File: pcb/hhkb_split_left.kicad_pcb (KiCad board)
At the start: 4 copper layers, 140.4 x 97.4 mm, 68 parts, among them SW1 Esc, SW10 E, SW11 R, SW12 T, SW13 Ctrl, SW14 A, SW15 S, SW16 D, SW17 F, SW18 G, SW19 Shift, SW2 1, SW20 Z, SW21 X, SW22 C, SW23 V, SW24 B, SW25 Alt, SW26 Meta, SW27 L-Space, SW3 2, SW4 3, SW5 4, SW6 5, SW7 Tab, SW8 Q, SW9 W, U1 74LVC595

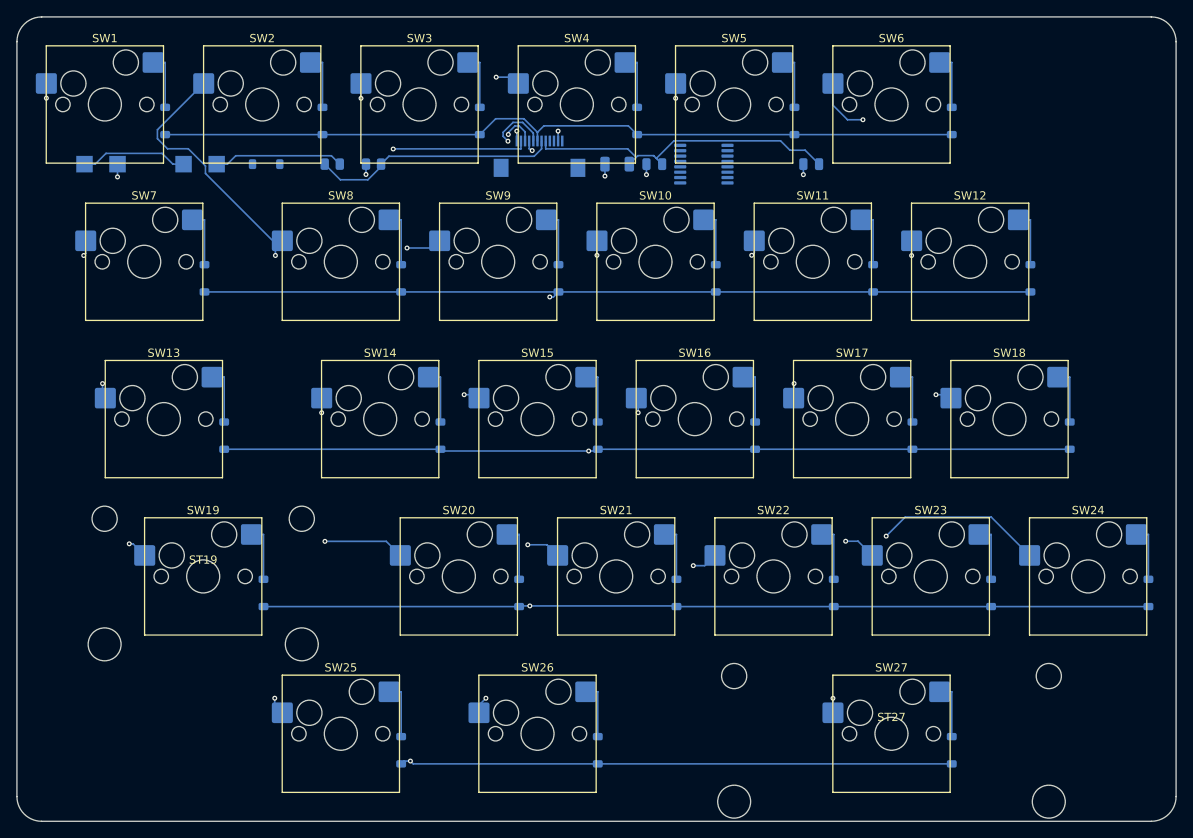
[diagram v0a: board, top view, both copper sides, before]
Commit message: マトリクスのダイオードを BAT46W にした（1N4148W はバックアップとして記録）
在庫 5,000 超の SOD-123 ショットキー 29 件、BAT47/48/49/54/85、1SS 系、
NSR、RB751、PMEG、MBR05xx、SS12、1N5711、BAS40 を当たった。
**VF と IR を両方「動作点で」保証しているのは BAT46W だけ。**

  BAT46W(C54110)  VF≦0.25V@0.1mA   IR≦0.3µA@1.5V   $6.76(122個+段取り)
  1N4148W(C81598) なし(1mA 0.715V) なし(20V 25nA)  $1.43 Basic
  SD103AW         0.37V@20mA       なし(30V 5µA)   $6.75
  BAT54W          240mV@0.1mA      なし(25V 2µA)   $6.25

罠: BAT48ZFILM-FS(C7436546) は名前だけで中身は SD103AW と同じ仕様。

## 効果

打ち止めがマイコン律速に戻る（1.20 → **1.10V/本**）。
**壊れ方が「一部のキーが反応しない」から「電源が落ちる」に変わる。**
実測が不要になる。

## 代償（数字で押さえた）

+約 ¥800。逆漏れ 12 倍で **60℃ かつ 5 個以上の同時押しだと余裕を割る**
（25℃ なら 9 個でも OK）。接合容量 5 倍だが列切替後 2.31µs に対し
SPI 転送で 4.0µs 以上空くので間に合う。

## 検査を 2 つ足した

  test_the_matrix_reads_high_at_the_cutoff … 打ち止めで行が VIH に届くか
  test_ghosting_survives_a_full_row_of_simultaneous_presses … 逆漏れの合計

どちらも故意に壊して検出を確認した。**1 回目は __pycache__ が古いまま
（同じ秒に書き換えたため）で検出できていなかった。**破壊試験のあとは
バイトコードを消すこと。

open-gaps #25 に「電池が尽きるときの止まり方」を記録した。マイコンの
ブラウンアウトは起動と広告を繰り返しうるし、**低電圧の flash 書き込みで
ペアリング情報が壊れうる**。POFCON か soft-off で自分から止めれば直るが、
ZMK に機能が無いので自作が要る。**基板に影響しないので届いてからでよい。**

3 基板とも DRC 0 / 未配線 0。検査 294 件。

Co-Authored-By: Claude Opus 5 (1M context) <noreply@anthropic.com>
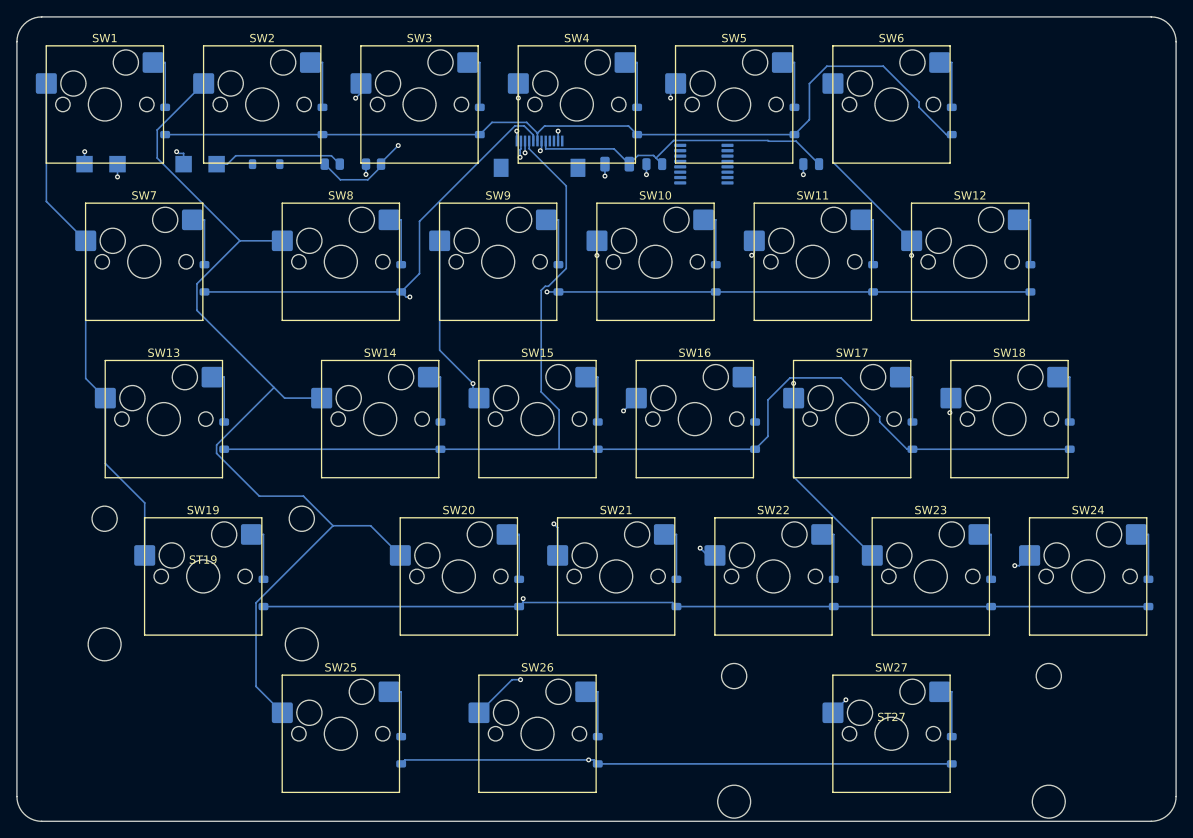
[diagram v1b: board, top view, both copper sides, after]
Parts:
- D1, D10, D11, D12, D13, D14, D15, D16, D17, D18, D19, D2, D20, D21, D22, D23, D24, D25, D26, D27, D3, D4, D5, D6, D7, D8, D9: value 1N4148W -> BAT46W
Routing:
- net COL1: track 104.3 -> 126.8 mm, vias 4 -> 0
- net COL2: track 74.7 -> 88.6 mm, vias 4 -> 3
- net ROW2: track 143.5 -> 154.1 mm, vias 2 -> 0
- net ROW0: track 98.5 -> 107.9 mm
- net ROW4: track 159.7 -> 151.4 mm
- net COL5: track 111.6 -> 104.9 mm, vias 5 -> 4
- net COL3: track 112.1 -> 105.6 mm
- net ROW3: track 174.0 -> 168.8 mm
- net COL0: track 66.1 -> 62.1 mm, vias 4 -> 0
- net COL4: track 71.6 -> 69.4 mm, vias 4 -> 3
- net VBATT_RAW: track 13.1 -> 14.9 mm, vias 0 -> 2
- net VBATT_SENSE: track 29.7 -> 30.4 mm, vias 0 -> 2

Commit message: #23 の D9 移設を実施した（アンテナ実外形の真下の配線が 0 本になった）
- ROW4 の行き先を D5（左列）→ D9（右列・元 MISO）へ。TX 側レーン 6 → 5 本、
  LANE_STEP 0.7 → 0.65。最内レーン -3.8mm はアンテナ実外形（-3.65〜-0.15）の外
- ケーブルのピン配置は ROW4 を右群 4 番へ（左群のままだと横枝が縦線を
  8 箇所で横切る。DRC で実測）。本体基板 2 枚も再生成＋再配線。3 基板 DRC 0
- ファームは row-gpios を D9 へ、&spi2_default/&spi2_sleep の psels から
  MISO を外して P1.14 を解放（CI ビルド・実機は未確認）
- 買い物リストを shopping-list.md に統合（#22 の再発防止の作法つき）
- Task C3 §6-6b に測定条件欄を追加
- 全検査 386 passed / 3 skipped

Co-Authored-By: Claude Fable 5 <noreply@anthropic.com>
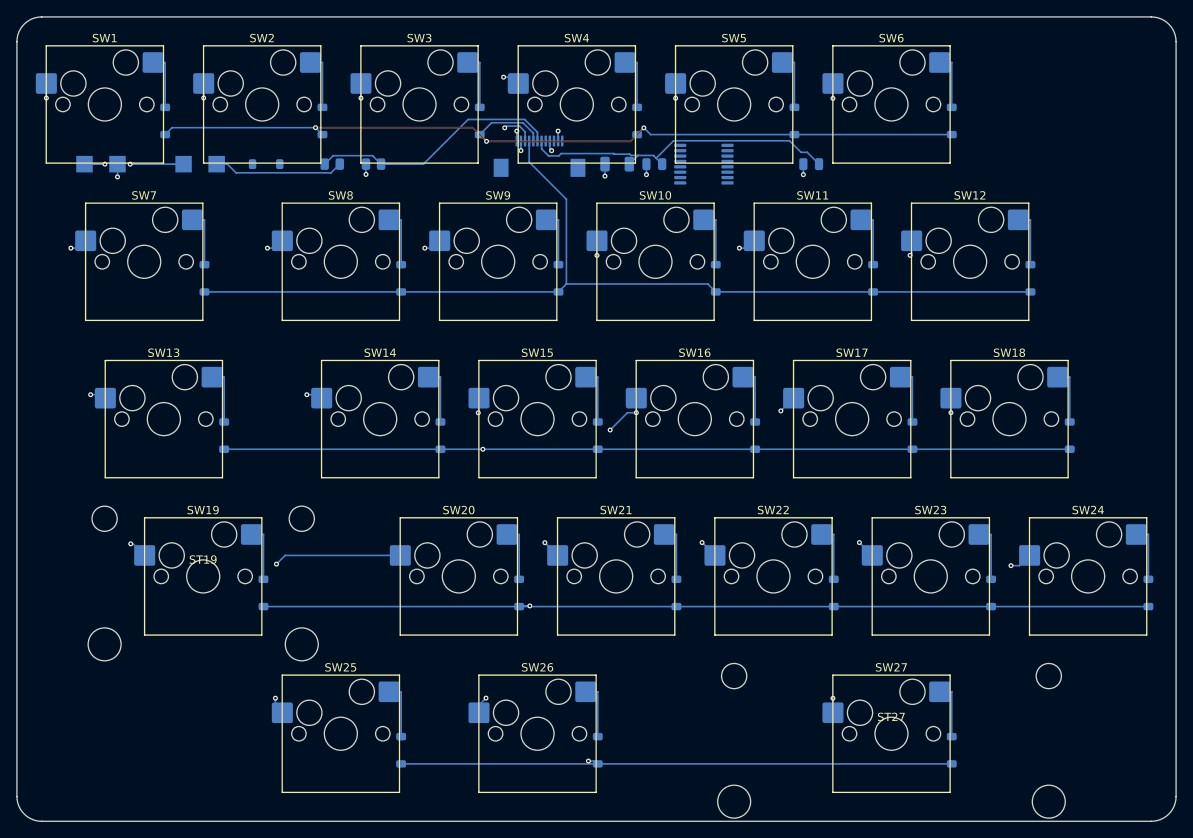
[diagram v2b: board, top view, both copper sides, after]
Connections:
- J_DB pad 10: ROW3 -> ROW2
- J_DB pad 11: ROW4 -> ROW3
- J_DB pad 4: SPI_MOSI -> ROW4
- J_DB pad 5: V3V3 -> SPI_MOSI
- J_DB pad 6: VBATT_SENSE -> V3V3
- J_DB pad 7: ROW0 -> VBATT_SENSE
- J_DB pad 8: ROW1 -> ROW0
- J_DB pad 9: ROW2 -> ROW1
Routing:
- net COL1: track 126.8 -> 102.9 mm, vias 0 -> 5
- net COL2: track 88.6 -> 71.1 mm, vias 3 -> 4
- net ROW1: track 129.7 -> 120.0 mm, vias 2 -> 0
- net COL3: track 105.6 -> 113.3 mm, vias 5 -> 6
- net ROW4: track 151.4 -> 156.9 mm
- net ROW2: track 154.1 -> 149.6 mm, vias 0 -> 2
- net COL0: track 62.1 -> 66.4 mm, vias 0 -> 4
- net VBATT_RAW: track 14.9 -> 12.0 mm
- net COL4: track 69.4 -> 71.4 mm, vias 3 -> 4
- net ROW0: track 107.9 -> 109.3 mm, vias 0 -> 3
- net V3V3: track 38.5 -> 39.8 mm
- net COL5: track 104.9 -> 103.6 mm, vias 4 -> 5
- net ROW3: track 168.8 -> 169.8 mm
- net VBATT_SENSE: track 30.4 -> 30.5 mm, vias 2 -> 0

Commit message: ★ 電池蓋を差し込み式にし、本体基板に固定を入れた（#35 / #36）
電池蓋（#35）: コブの奥面へ移し、留め方を 3 度作り直した。片持ちばね案は
**原理的に外れない**（腕が壁の裏に立っていて、どう撓ませても抜けない。
逃がす先の内側は電池が埋めている）。断面を描いて分かった。採用したのは
下へスライドして庇の裏へ舌を差し込む形で、重力が留める側に効く。
検査は「留まる」と「外せる」を必ず一緒に見る——前者だけでは不成立案が通った。

本体基板（#36）: 取付穴 6/8 とプレート裏の柱・M2 ネジ。穴の探索が
コートヤードしか見ておらず、柱がキーとプレート開口に当たっていた。
柱の検査は assert がループの中にあって 1 本目で止まっており、3 往復した。

その他: 自動配線器がたまに 0.12mm の線を引いて DRC が赤になるので、
取り込み後に幅を揃えるようにした（配線するたびに赤が出たり出なかったり
していた）。CAD を変えたら絵を出し直す手順を tools/refresh_view.sh に。

検査 395 件 緑 / DRC 3 基板とも 0 違反・0 未配線

Co-Authored-By: Claude Opus 5 (1M context) <noreply@anthropic.com>
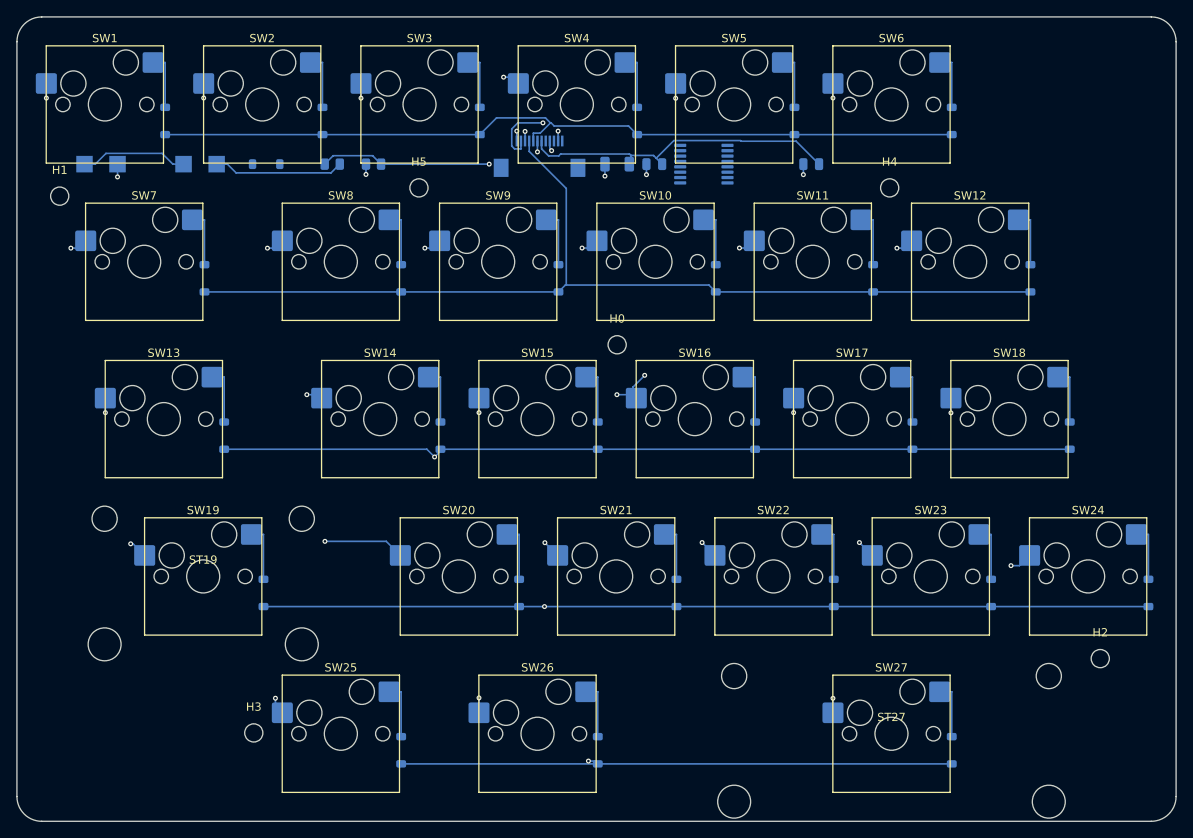
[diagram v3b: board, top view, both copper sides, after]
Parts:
- added H0: MountingHole_2.2mm_M2, MountingHole_2.2mm_M2, F.Cu at (152.5, 91.0)
- added H1: MountingHole_2.2mm_M2, MountingHole_2.2mm_M2, F.Cu at (85.0, 73.0)
- added H2: MountingHole_2.2mm_M2, MountingHole_2.2mm_M2, F.Cu at (211.0, 129.0)
- added H3: MountingHole_2.2mm_M2, MountingHole_2.2mm_M2, F.Cu at (108.5, 138.0)
- added H4: MountingHole_2.2mm_M2, MountingHole_2.2mm_M2, F.Cu at (185.5, 72.0)
- added H5: MountingHole_2.2mm_M2, MountingHole_2.2mm_M2, F.Cu at (128.5, 72.0)
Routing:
- net COL2: track 71.1 -> 80.7 mm
- net ROW0: track 109.3 -> 100.5 mm, vias 3 -> 0
- net ROW3: track 169.8 -> 177.3 mm
- net COL1: track 102.9 -> 99.1 mm
- net VBATT_SENSE: track 30.5 -> 28.5 mm, vias 0 -> 2
- net VBATT_RAW: track 12.0 -> 13.1 mm, vias 2 -> 0
- net COL3: track 113.3 -> 114.1 mm

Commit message: 2 層化と GND ベタ両面化、GND ビアの大量投入（指摘 2/3/4/5/8）
**まだ未配線が残っている途中状態**（左 1・右 3）。DRC 違反は 3 基板とも 0。

指摘 2（2 層化）
  4 層にした当時の根拠「行の引き回しが 2 層では通らない」は、その後
  Freerouting に切り替えたときに崩れていた。実測すると信号は In2.Cu と
  B.Cu の 2 層に収まり、**F.Cu は配線 0 本で丸ごと空いていた。**
  決定記録がその事実に追いついていなかった。

指摘 3（GND ベタ）
  F.Cu と B.Cu の両面に敷いた。4 層のときのように GND 専用層を
  自動配線器から予約することはできない（信号層と兼ねるため）。

指摘 4/5（GND ビア）
  ファンアウト（パッド→地板）に加えて 2 種類足した。

    格子状のスティッチング   左 175 / 右 210
    長い配線の脇のビアフェンス 左 121 / 右 174

  **ビアフェンスの目的は離島の救済ではない。**信号の戻り電流は配線の
  直近を流れたがるが、長い配線がベタを割ると、戻り電流はスリットの端まで
  大回りするしかない。配線をまたぐ位置にビアがあれば、反対面を経由して
  その場で横断できる。「繋がっている」と「最短で行ける」は別。

指摘 8（電源を太く）
  **ネットクラスを 2 つに割った**（KiCad は複数クラスを DSN に書き出し、
  Freerouting も受け取る。生の DSN を読んで確認した）。

    PowerFFC   V3V3       0.30mm  ← FFC のパッドが 0.30mm 幅で、これが上限
    PowerWide  GND ほか   0.60mm  ← 細ピッチのパッドに繋がらないので太くできる

  当初 0.5mm 一律にしたら V3V3 が J_DB に届かず未配線になった。
  測ったら Hirose FH12-12S-0.5SH のパッドは幅 0.30mm・隙間 0.20mm で、
  **0.5mm の線は物理的に載らない。**

自分のコードで踏んだ落とし穴（どれも実測で見つけた）
  - `pad is skip` で自分を除外 → SWIG は毎回別プロキシを返すので効かず、
    ファンアウトが 0 個になった
  - 箱どうしの重なりで当たり判定 → 丸いビアには厳しすぎ、0.65mm ピッチの
    TSSOP でビアが 1 つも置けなかった
  - **フットプリントの外接箱を障害物にした** → MX スイッチが約 19mm 角
    あるため基板全面が「置けない」ことになり、格子点の 8 割が飛んだ。
    実際に妨げるのはパッドと穴なので、そちらで見るようにした
  - ビア半径を二重に数えていた（0.3mm 過剰に保守的）→ 10.8mm² の離島でも
    格子点 48 個が全部「置けない」判定だった

配線後に 1 本ずつ太らせる後処理（gnd_fanout.widen）は**外した。**
自前の当たり判定が取りこぼして DRC 違反を 3 回続けて出したのと、
指摘 8 はクラス分けで達成できているため。実装は残してある。

Co-Authored-By: Claude Sonnet 5 <noreply@anthropic.com>
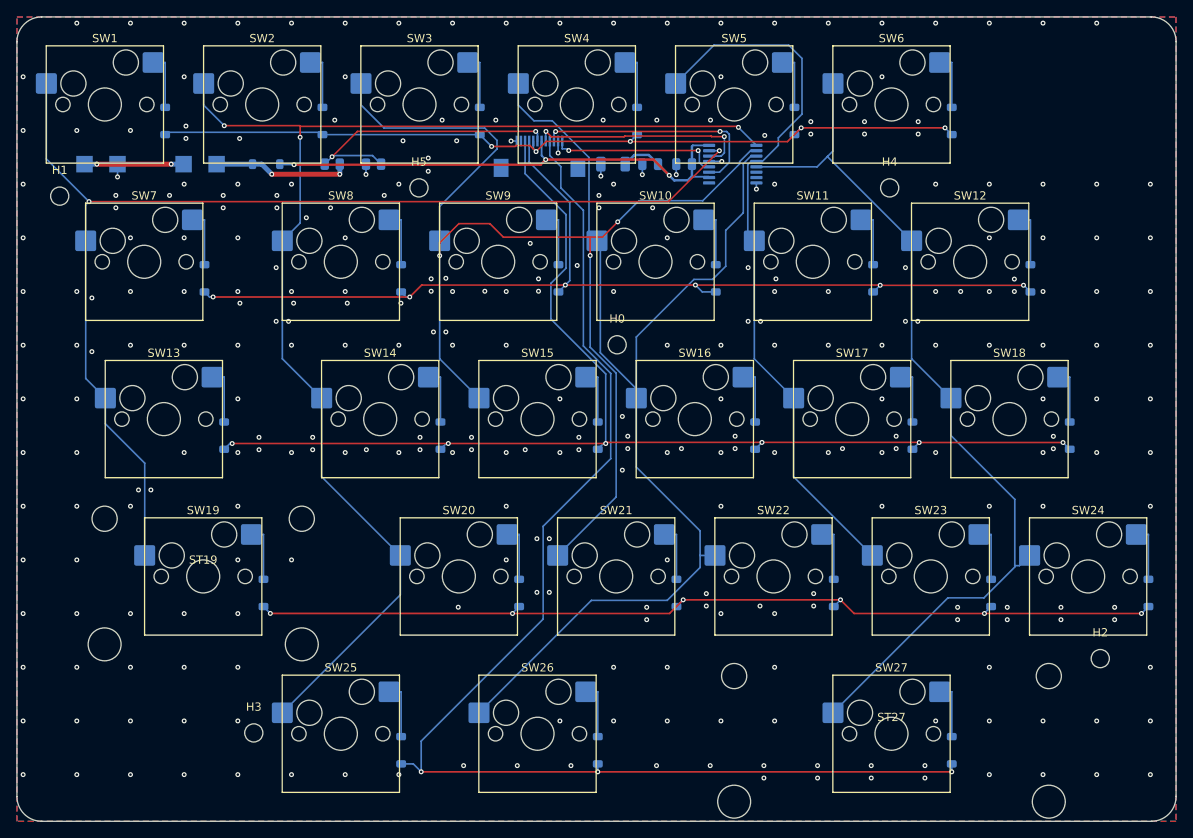
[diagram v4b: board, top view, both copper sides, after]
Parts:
- removed C_MCU: cap_100n, C_0805_2012Metric
- added C_RAIL: cap_100n, C_0805_2012Metric, B.Cu at (156.5, 69.1)
- moved C_U1 15.4 mm to (160.6, 69.1)
- moved U1 3.50 mm to (166.5, 69.1)
- moved C_BULK 0.50 mm to (152.0, 69.1)
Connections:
- D_PWR pad 1: (no net) -> V3V3
- D_PWR pad 2: (no net) -> VBATT_SW
- U1 pad 1: (no net) -> COL1
- U1 pad 10: (no net) -> V3V3
- U1 pad 11: (no net) -> SPI_SCK
- U1 pad 12: (no net) -> CS
- U1 pad 13: (no net) -> GND
- U1 pad 14: (no net) -> SPI_MOSI
- U1 pad 15: (no net) -> COL0
- U1 pad 16: (no net) -> V3V3
- U1 pad 2: (no net) -> COL2
- U1 pad 3: (no net) -> COL3
- U1 pad 4: (no net) -> COL4
- U1 pad 5: (no net) -> COL5
- U1 pad 8: (no net) -> GND
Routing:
- net COL0: track 66.5 -> 142.5 mm, vias 4 -> 2
- net COL2: track 80.7 -> 145.7 mm, vias 4 -> 3
- net ROW3: track 177.3 -> 113.9 mm, vias 2 -> 6
- net COL1: track 99.1 -> 155.3 mm, vias 5 -> 3
- net V3V3: track 39.4 -> 68.6 mm, vias 0 -> 3
- net SPI_SCK: track 0.00 -> 28.8 mm, vias 0 -> 2
- net COL3: track 114.1 -> 141.9 mm, vias 6 -> 0
- net SPI_MOSI: track 0.00 -> 27.1 mm, vias 0 -> 2
- net CS: track 0.00 -> 20.4 mm, vias 0 -> 2
- net COL4: track 70.9 -> 87.8 mm, vias 4 -> 0
- net ROW1: track 120.0 -> 127.4 mm, vias 0 -> 6
- net VBATT_SENSE: track 28.5 -> 34.9 mm
- net COL5: track 104.0 -> 109.0 mm, vias 5 -> 0
- net GND: track 9.20 -> 11.2 mm, vias 7 -> 305
- net ROW0: track 100.5 -> 101.7 mm, vias 0 -> 5
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- added copper zone on B.Cu, net GND
- added copper zone on F.Cu, net GND
- removed copper zone on In1.Cu, net GND
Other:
- copper layers 4 -> 2

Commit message: 閾値を設計規則から導き、「厳しすぎ」を検出する検査を足した
利用者の問い「その閾値はヒューリスティックか。妥当か。例外はないか」への対応。

**問題は「緩すぎ」ではなく「厳しすぎ」だった。**
DRC は規則より緩ければ必ず捕まえる（無条件に太らせて 47 件出ることを
故意に壊して確認済み）。だが**規則より厳しく置いても DRC は緑のまま**で、
ビアが減っていても誰も気づけない。実際そうなっていた。

  - クリアランス 0.2 を**数値リテラルで 4 か所**に持っていた。
    設計規則を変えても追随しない
  - ビアの半径を二重に数えていて 0.3mm 過剰に厳しく、
    **10.8mm² の離島でも格子点 48 個が全部「置けない」判定**だった

直した内容:

  - `_clearance_mm(board)` が基板の設計規則から読む。**数値を書かない**
  - `_via_keepout_mm(board)` = ビア半径 + クリアランス + 余裕。
    判断で置いた数字は `SAFETY_MM = 0.05` だけ（丸めと矩形近似の保険）
  - **結果の量を測る検査**を足した。「厳しすぎ」はここでしか見つからない

        test_there_are_enough_ground_vias_to_tie_the_two_planes
        test_few_pieces_of_ground_copper_are_left_floating

効果（判定を直したことによる実測の変化）:

    浮いた GND の区画   左 15 → 4   右 14 → 5
    GND ビアの総数      左 305 → 342   右 396 → 423

**設計規則の数値を tools/pcb_rules.py へ出した。**
gen_pcb は `import pcbnew` するので KiCad の Python でしか読めず、
母艦の venv で動く検査から参照すると ModuleNotFoundError で落ちる。
（`part_kinds.py` を作ったのと同じ理由）

**電源をクラスの幅まで後から引き上げるのはやめた。**
一度やったら DRC 違反が増えた（左 0→1・右 1→2）。分布を測ると:

    VBATT_RAW / VBATT_SW   100% が 0.60mm
    V3V3                   97%（254/261）が 0.30mm、狭い 7 区間だけ 0.225mm

**Freerouting は狭いところで自分から幅を絞っている。**利用者が求めた
「太くできるところは太く、できないところはしない」を自動配線器が
既にやっており、後から一律に太らせるのはその判断を壊す行為だった。

検査側の不具合も 1 つ直した。KiCad 10 はビアのネットを `(net "COL0")` と
**名前**で書く（番号ではない）。番号を期待した正規表現が 1 件も拾えず
「GND のビアが 0 個」という嘘の赤を出していた。S 式を正規表現で読むのを
やめ、pcbnew から取るようにした。

4 層前提の `test_the_ground_stays_one_island_after_routing` は削除。
2 層では信号層とベタが同じ面を兼ねるので**面が割れるのは避けられず、
「島が 1 つ」は達成し得ない条件**になった。割れていてもビアで
繋がっていればよいので、浮いた区画の数で見る検査に置き換えた。

Co-Authored-By: Claude Sonnet 5 <noreply@anthropic.com>
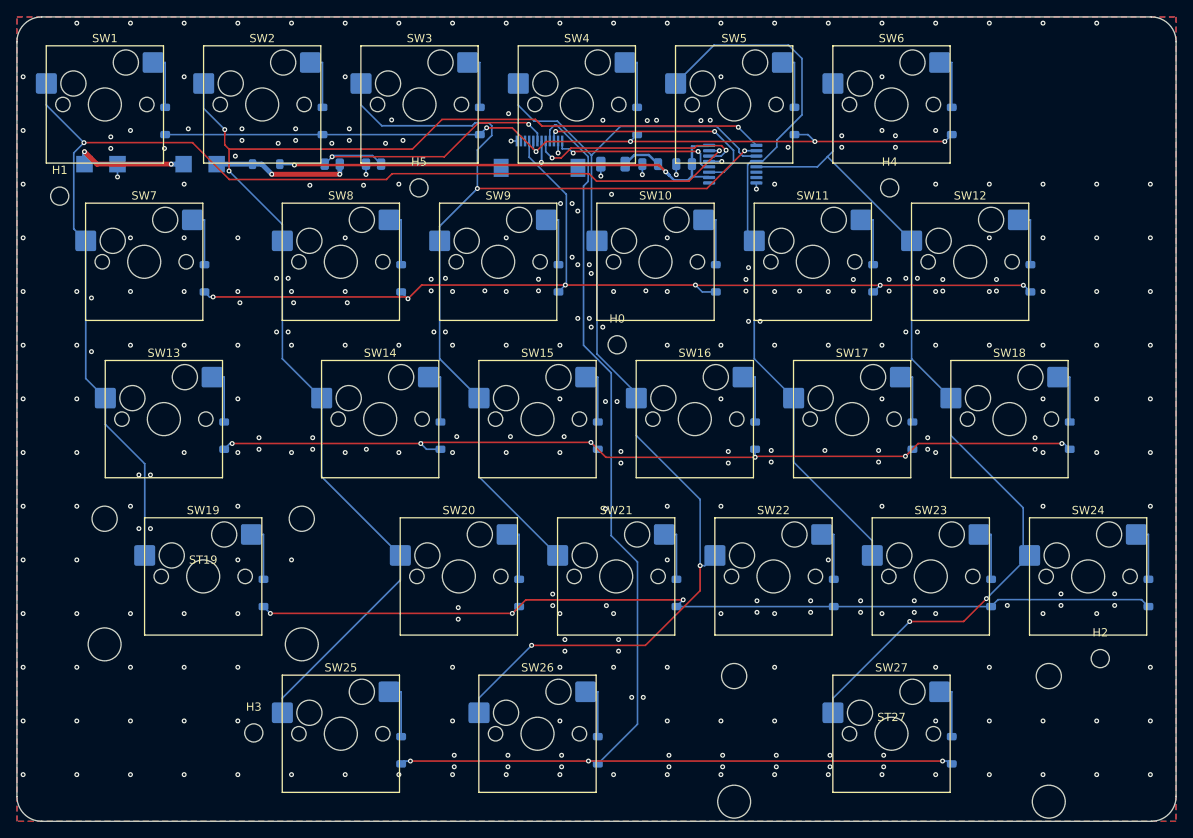
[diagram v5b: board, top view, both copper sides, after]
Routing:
- net ROW2: track 150.1 -> 110.5 mm
- net COL2: track 145.7 -> 116.0 mm, vias 3 -> 2
- net COL3: track 141.9 -> 131.6 mm, vias 0 -> 2
- net ROW4: track 157.9 -> 154.5 mm
- net COL1: track 155.3 -> 158.6 mm
- net COL0: track 142.5 -> 145.3 mm
- net VBATT_RAW: track 12.0 -> 14.1 mm
- net ROW3: track 113.9 -> 112.0 mm, vias 6 -> 3
- net ROW0: track 101.7 -> 103.1 mm
- net VBATT_SENSE: track 34.9 -> 35.7 mm
- net COL5: track 109.0 -> 109.5 mm, vias 0 -> 2
- net GND: vias 305 -> 343
